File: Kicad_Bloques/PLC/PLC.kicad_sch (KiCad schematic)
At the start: 3 parts, among them J1 Conn_01x18_Socket, J2 Conn_01x18_Socket, U1 ESP32-S3-WROOM-1

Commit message: Actualizacion bloques 9/2/2026{
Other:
- sheet Fuente ports: added 12v, 24v, 5v; removed none
- sheet Relay_Block ports: added 24V, 5v, Out_R_NC, Out_R_NO, R_Signal1; removed none
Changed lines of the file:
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@@
 	(generator_version "9.0")
 	(paper "A4")
+	(wire
+		(pts
+			(xy 163.83 139.7) (xy 166.37 139.7)
+		)
+		(stroke
+			(width 0)
+			(type default)
+		)
+	)
+	(wire
+		(pts
+			(xy 81.28 41.91) (xy 82.55 41.91)
+		)
+		(stroke
+			(width 0)
+			(type default)
+		)
+	)
+	(wire
+		(pts
+			(xy 163.83 137.16) (xy 166.37 137.16)
+		)
+		(stroke
+			(width 0)
+			(type default)
+		)
+	)
+	(wire
+		(pts
+			(xy 81.28 39.37) (xy 82.55 39.37)
+		)
+		(stroke
+			(width 0)
+			(type default)
+		)
+	)
+	(wire
+		(pts
+			(xy 163.83 134.62) (xy 166.37 134.62)
+		)
+		(stroke
+			(width 0)
+			(type default)
+		)
+	)
+	(label "12v"
+		(at 166.37 137.16 0)
+		(effects
+			(font
+				(size 1.27 1.27)
+			)
+			(justify left bottom)
+		)
+	)
+	(label "5v"
+		(at 166.37 139.7 0)
+		(effects
+			(font
+				(size 1.27 1.27)
+			)
+			(justify left bottom)
+		)
+	)
+	(label "24v"
+		(at 166.37 134.62 0)
+		(effects
+			(font
+				(size 1.27 1.27)
+			)
+			(justify left bottom)
+		)
+	)
+	(label "24v"
+		(at 81.28 41.91 180)
+		(effects
+			(font
+				(size 1.27 1.27)
+			)
+			(justify right bottom)
+		)
+	)
+	(label "5v"
+		(at 81.28 39.37 180)
+		(effects
+			(font
+				(size 1.27 1.27)
+			)
+			(justify right bottom)
+		)
+	)
 	(symbol
 		(lib_id "RF_Module:ESP32-S3-WROOM-1")
@@
 			)
 		)
+		(pin "24v" output
+			(at 163.83 134.62 0)
+			(effects
+				(font
+					(size 1.27 1.27)
+				)
+				(justify right)
+			)
+		)
+		(pin "5v" output
+			(at 163.83 139.7 0)
+			(effects
+				(font
+					(size 1.27 1.27)
+				)
+				(justify right)
+			)
+		)
+		(pin "12v" output
+			(at 163.83 137.16 0)
+			(effects
+				(font
+					(size 1.27 1.27)
+				)
+				(justify right)
+			)
+		)
 		(instances
 			(project "PLC"
@@
 			)
 		)
+		(pin "Out_R_NO" output
+			(at 106.68 41.91 0)
+			(effects
+				(font
+					(size 1.27 1.27)
+				)
+				(justify right)
+			)
+		)
+		(pin "Out_R_NC" output
+			(at 106.68 44.45 0)
+			(effects
+				(font
+					(size 1.27 1.27)
+				)
+				(justify right)
+			)
+		)
+		(pin "R_Signal1" input
+			(at 82.55 44.45 180)
+			(effects
+				(font
+					(size 1.27 1.27)
+				)
+				(justify left)
+			)
+		)
+		(pin "5v" input
+			(at 82.55 39.37 180)
+			(effects
+				(font
+					(size 1.27 1.27)
+				)
+				(justify left)
+			)
+		)
+		(pin "24V" input
+			(at 82.55 41.91 180)
+			(effects
+				(font
+					(size 1.27 1.27)
+				)
+				(justify left)
+			)
+		)

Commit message: Actualizacion Bloques e Investigacion
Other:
- sheet Digital_block ports: added 3.3v, Digital_S1, Out_D1; removed none
- sheet Fuente ports: added 3.3v; removed none
- sheet Relay_Block ports: added Out_Relay; removed 24V, Out_R_NC, Out_R_NO, R_Signal1
- moved on the sheet: J1
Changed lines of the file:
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@@
 	(wire
 		(pts
-			(xy 163.83 139.7) (xy 166.37 139.7)
+			(xy 163.83 138.43) (xy 166.37 138.43)
 		)
 		(stroke
@@
 	(wire
 		(pts
-			(xy 81.28 41.91) (xy 82.55 41.91)
+			(xy 163.83 135.89) (xy 166.37 135.89)
 		)
 		(stroke
@@
 	(wire
 		(pts
-			(xy 163.83 137.16) (xy 166.37 137.16)
+			(xy 74.93 39.37) (xy 76.2 39.37)
 		)
 		(stroke
@@
 	(wire
 		(pts
-			(xy 81.28 39.37) (xy 82.55 39.37)
+			(xy 163.83 140.97) (xy 166.37 140.97)
 		)
 		(stroke
@@
 	(wire
 		(pts
-			(xy 163.83 134.62) (xy 166.37 134.62)
+			(xy 163.83 133.35) (xy 166.37 133.35)
 		)
 		(stroke
@@
 		)
 	)
+	(wire
+		(pts
+			(xy 144.78 41.91) (xy 147.32 41.91)
+		)
+		(stroke
+			(width 0)
+			(type default)
+		)
+	)
 	(label "12v"
-		(at 166.37 137.16 0)
+		(at 166.37 135.89 0)
 		(effects
 			(font
@@
 	)
 	(label "5v"
-		(at 166.37 139.7 0)
+		(at 166.37 138.43 0)
 		(effects
 			(font
@@
 	)
 	(label "24v"
-		(at 166.37 134.62 0)
+		(at 166.37 133.35 0)
 		(effects
 			(font
@@
 		)
 	)
-	(label "24v"
-		(at 81.28 41.91 180)
+	(label "3.3v"
+		(at 144.78 41.91 180)
 		(effects
 			(font
 				(size 1.27 1.27)
+				(thickness 0.1588)
 			)
 			(justify right bottom)
@@
 	)
 	(label "5v"
-		(at 81.28 39.37 180)
+		(at 74.93 39.37 180)
 		(effects
 			(font
@@
 			)
 			(justify right bottom)
+		)
+	)
+	(label "3.3v"
+		(at 166.37 140.97 0)
+		(effects
+			(font
+				(size 1.27 1.27)
+				(thickness 0.1588)
+			)
+			(justify left bottom)
 		)
 	)
@@
 		(on_board yes)
 		(dnp no)
-		(fields_autoplaced yes)
 		(property "Reference" "U1"
-			(at 121.5233 62.23 0)
+			(at 119.888 63.5 0)
 			(effects
 				(font
@@
 		)
 		(property "Value" "ESP32-S3-WROOM-1"
-			(at 121.5233 64.77 0)
+			(at 119.888 66.04 0)
 			(effects
 				(font
@@
 	(symbol
 		(lib_id "Connector:Conn_01x18_Socket")
-		(at 148.59 91.44 0)
+		(at 151.13 91.44 0)
 		(unit 1)
 		(exclude_from_sim no)
@@
 		(on_board yes)
 		(dnp no)
-		(fields_autoplaced yes)
 		(property "Reference" "J1"
-			(at 149.86 91.4399 0)
+			(at 148.082 66.548 0)
 			(effects
 				(font
@@
 		)
 		(property "Value" "Conn_01x18_Socket"
-			(at 149.86 93.9799 0)
+			(at 139.954 68.58 0)
 			(effects
 				(font
@@
 		)
 		(property "Footprint" ""
-			(at 148.59 91.44 0)
+			(at 151.13 91.44 0)
 			(effects
 				(font
@@
 		)
 		(property "Datasheet" "~"
-			(at 148.59 91.44 0)
+			(at 151.13 91.44 0)
 			(effects
 				(font
@@
 		)
 		(property "Description" "Generic connector, single row, 01x18, script generated"
-			(at 148.59 91.44 0)
+			(at 151.13 91.44 0)
 			(effects
 				(font
@@
 		)
 		(pin "24v" output
-			(at 163.83 134.62 0)
+			(at 163.83 133.35 0)
 			(effects
 				(font
@@
 		)
 		(pin "5v" output
-			(at 163.83 139.7 0)
+			(at 163.83 138.43 0)
 			(effects
 				(font
@@
 		)
 		(pin "12v" output
-			(at 163.83 137.16 0)
+			(at 163.83 135.89 0)
+			(effects
+				(font
+					(size 1.27 1.27)
+				)
+				(justify right)
+			)
+		)
+		(pin "3.3v" output
+			(at 163.83 140.97 0)
 			(effects
 				(font
@@
 	)
 	(sheet
-		(at 137.16 36.83)
+		(at 147.32 36.83)
 		(size 25.4 12.7)
 		(exclude_from_sim no)
@@
 		)
 		(property "Sheetname" "Digital_block"
-			(at 137.16 36.1184 0)
+			(at 147.32 36.1184 0)
 			(effects
 				(font
@@
 		)
 		(property "Sheetfile" "Digital.kicad_sch"
-			(at 137.16 50.1146 0)
+			(at 147.32 50.1146 0)
 			(effects
 				(font
@@
 				)
 				(justify left top)
+			)
+		)
+		(pin "Out_D1" output
+			(at 172.72 41.91 0)
+			(effects
+				(font
+					(size 1.27 1.27)
+				)
+				(justify right)
+			)
+		)
+		(pin "Digital_S1" input
+			(at 147.32 44.45 180)
+			(effects
+				(font
+					(size 1.27 1.27)
+				)
+				(justify left)
+			)
+		)
+		(pin "3.3v" input
+			(at 147.32 41.91 180)
+			(effects
+				(font
+					(size 1.27 1.27)
+				)
+				(justify left)
 			)
 		)
@@
 	)
 	(sheet
-		(at 82.55 36.83)
+		(at 76.2 36.83)
 		(size 24.13 12.7)
 		(exclude_from_sim no)
@@
 		)
 		(property "Sheetname" "Relay_Block"
-			(at 82.55 36.1184 0)
+			(at 76.2 36.1184 0)
 			(effects
 				(font
@@
 		)
 		(property "Sheetfile" "Relay.kicad_sch"
-			(at 82.55 50.1146 0)
+			(at 76.2 50.1146 0)
 			(effects
 				(font
@@
 			)
 		)
-		(pin "Out_R_NO" output
-			(at 106.68 41.91 0)
-			(effects
-				(font
-					(size 1.27 1.27)
-				)
-				(justify right)
-			)
-		)
-		(pin "Out_R_NC" output
-			(at 106.68 44.45 0)
-			(effects
-				(font
-					(size 1.27 1.27)
-				)
-				(justify right)
-			)
-		)
-		(pin "R_Signal1" input
-			(at 82.55 44.45 180)
+		(pin "5v" input
+			(at 76.2 39.37 180)
 			(effects
 				(font
@@
 			)
 		)
-		(pin "5v" input
-			(at 82.55 39.37 180)
-			(effects
-				(font
-					(size 1.27 1.27)
-				)
-				(justify left)
-			)
-		)
-		(pin "24V" input
-			(at 82.55 41.91 180)
-			(effects
-				(font
+		(pin "Out_Relay" input
+			(at 76.2 44.45 180)
+			(effects
+				(font

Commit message: Bloque Analogico
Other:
- sheet 0-10V_Block ports: added 0-10v, 3.3v, Out_Analogic; removed none
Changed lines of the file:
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@@
 	(wire
 		(pts
-			(xy 144.78 41.91) (xy 147.32 41.91)
+			(xy 139.7 41.91) (xy 142.24 41.91)
 		)
 		(stroke
@@
 	)
 	(label "3.3v"
-		(at 144.78 41.91 180)
+		(at 139.7 41.91 180)
 		(effects
 			(font
@@
 	)
 	(sheet
-		(at 147.32 36.83)
+		(at 142.24 36.83)
 		(size 25.4 12.7)
 		(exclude_from_sim no)
@@
 		)
 		(property "Sheetname" "Digital_block"
-			(at 147.32 36.1184 0)
+			(at 142.24 36.1184 0)
 			(effects
 				(font
@@
 		)
 		(property "Sheetfile" "Digital.kicad_sch"
-			(at 147.32 50.1146 0)
+			(at 142.24 50.1146 0)
 			(effects
 				(font
@@
 		)
 		(pin "Out_D1" output
-			(at 172.72 41.91 0)
+			(at 167.64 41.91 0)
 			(effects
 				(font
@@
 		)
 		(pin "Digital_S1" input
-			(at 147.32 44.45 180)
+			(at 142.24 44.45 180)
 			(effects
 				(font
@@
 		)
 		(pin "3.3v" input
-			(at 147.32 41.91 180)
+			(at 142.24 41.91 180)
 			(effects
 				(font
@@
 			)
 		)
+		(pin "3.3v" input
+			(at 110.49 137.16 180)
+			(effects
+				(font
+					(size 1.27 1.27)
+				)
+				(justify left)
+			)
+		)
+		(pin "Out_Analogic" output
+			(at 135.89 137.16 0)
+			(effects
+				(font
+					(size 1.27 1.27)
+				)
+				(justify right)
+			)
+		)
+		(pin "0-10v" input
+			(at 110.49 139.7 180)
+			(effects
+				(font
+					(size 1.27 1.27)
+				)
+				(justify left)
+			)
+		)

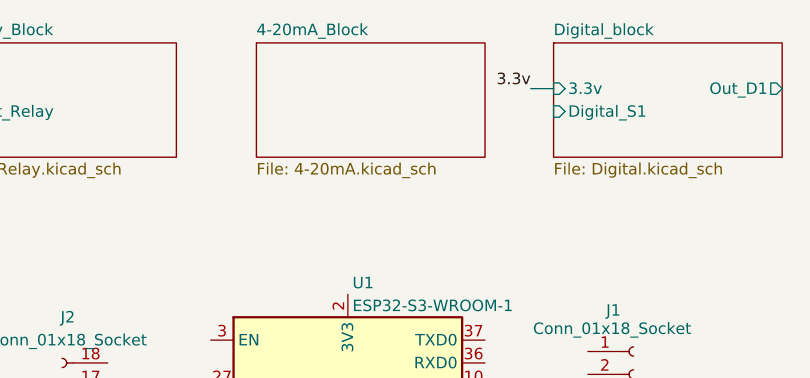
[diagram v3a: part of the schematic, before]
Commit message: Actualizacion bloque 4-20mA
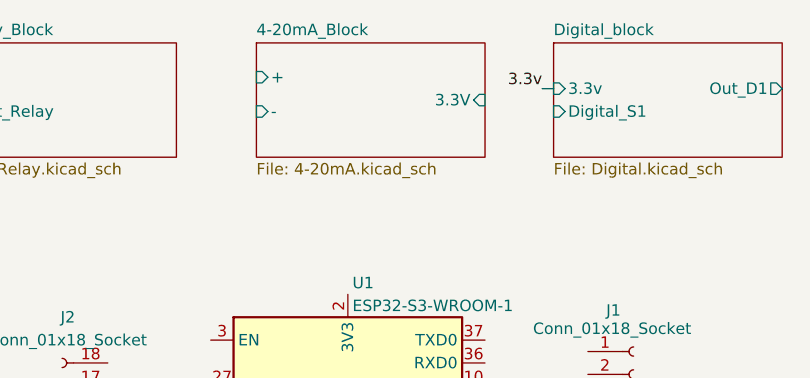
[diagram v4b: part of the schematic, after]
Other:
- sheet 4-20mA_Block ports: added +, -, 3.3V; removed none
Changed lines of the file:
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@@
 	(wire
 		(pts
-			(xy 139.7 41.91) (xy 142.24 41.91)
+			(xy 140.97 41.91) (xy 142.24 41.91)
 		)
 		(stroke
@@
 	)
 	(label "3.3v"
-		(at 139.7 41.91 180)
+		(at 140.97 41.91 180)
 		(effects
 			(font
@@
 			)
 		)
+		(pin "-" input
+			(at 109.22 44.45 180)
+			(effects
+				(font
+					(size 1.27 1.27)
+				)
+				(justify left)
+			)
+		)
+		(pin "+" input
+			(at 109.22 40.64 180)
+			(effects
+				(font
+					(size 1.27 1.27)
+				)
+				(justify left)
+			)
+		)
+		(pin "3.3V" input
+			(at 134.62 43.18 0)
+			(effects
+				(font
+					(size 1.27 1.27)
+				)
+				(justify right)
+			)
+		)

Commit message: Actualizacion de bloques
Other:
- sheet 4-20mA_Block ports: added Output_4-20mA; removed none
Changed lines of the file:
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@@
+	(wire
+		(pts
+			(xy 134.62 43.18) (xy 140.97 43.18)
+		)
+		(stroke
+			(width 0)
+			(type default)
+		)
+	)
 	(wire
 		(pts
 			(xy 163.83 135.89) (xy 166.37 135.89)
+		)
+		(stroke
+			(width 0)
+			(type default)
+		)
+	)
+	(wire
+		(pts
+			(xy 140.97 43.18) (xy 140.97 41.91)
 		)
 		(stroke
@@
 			(effects
 				(font
+					(size 1.27 1.27)
+				)
+				(justify right)
+			)
+		)
+		(pin "Output_4-20mA" output
+			(at 134.62 45.72 0)
+			(effects
+				(font
